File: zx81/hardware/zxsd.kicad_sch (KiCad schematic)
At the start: 37 parts, among them J1 Micro_SD_Card, J2 ZX81_EXP, SW1 RESET, U1 74HCT32, U10 27C256, U11 KM62256CLP, U12 74HCT08, U2 74HCT32, U3 74HCT00, U4 74HCT04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

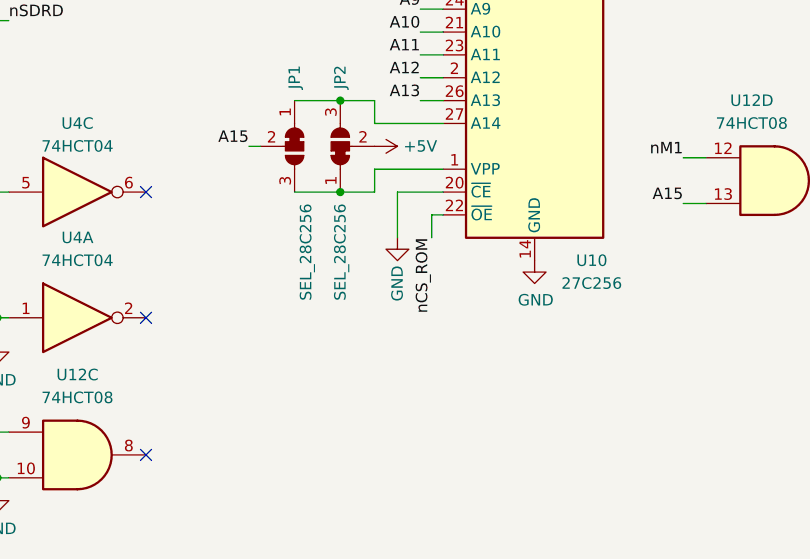
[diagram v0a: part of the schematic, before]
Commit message: re-used ROM's /CE for address decoder, /RD is connected to /OE now
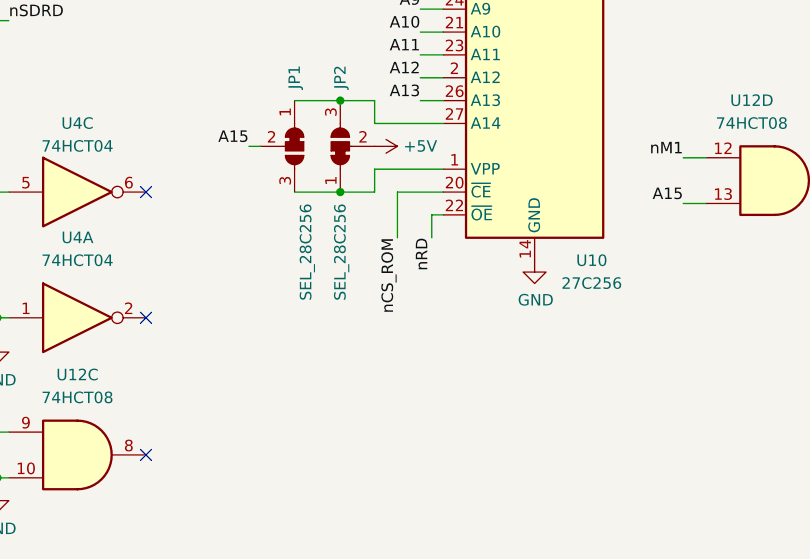
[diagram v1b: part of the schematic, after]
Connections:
- net GND: no longer U10.20 (~{CE})
- net nCS_ROM: now also U10.20 (~{CE}); no longer U10.22 (~{OE})
- net nRD: now also U10.22 (~{OE})
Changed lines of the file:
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@@
     (effects (font (size 1.27 1.27)) (justify left bottom))
   )
-  (label "nCS_ROM" (at 196.85 154.94 270)
+  (label "nCS_ROM" (at 193.04 154.94 270)
     (effects (font (size 1.27 1.27)) (justify right bottom))
   )
@@
   )
   (label "D4" (at 121.92 125.73 180)
+    (effects (font (size 1.27 1.27)) (justify right bottom))
+  )
+  (label "nRD" (at 196.85 154.94 270)
     (effects (font (size 1.27 1.27)) (justify right bottom))
   )
@@
     (pin "1")
   )
-  (symbol (lib_id "power:GND") (at 193.04 154.94 0) (unit 1)
-    (in_bom yes) (on_board yes)
-    (property "Reference" "#PWR0125" (id 0) (at 193.04 161.29 0)
-      (effects (font (size 1.27 1.27)) hide)
-    )
-    (property "Value" "GND" (id 1) (at 193.04 160.02 90))
-    (property "Footprint" "" (id 2) (at 193.04 154.94 0)
-      (effects (font (size 1.27 1.27)) hide)
-    )
-    (property "Datasheet" "" (id 3) (at 193.04 154.94 0)
-      (effects (font (size 1.27 1.27)) hide)
-    )
-    (pin "1")
-  )
   (symbol (lib_id "Regulator_Linear:MCP1700x-330xxTO") (at 86.36 49.53 0) (mirror x) (unit 1)
     (in_bom yes) (on_board yes) (fields_autoplaced)
@@
       (reference "#PWR0124") (unit 1) (value "GND") (footprint "")
     )
-    (path "/ba6f9c95-ca6f-4eb9-8074-0942ae88df92"
-      (reference "#PWR0125") (unit 1) (value "GND") (footprint "")
-    )
     (path "/a0f7f3a3-3c90-43d8-8b43-5a00494289e5"
